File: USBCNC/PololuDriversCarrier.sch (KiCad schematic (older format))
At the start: 10 parts, among them M1 Pololu_A4988, M2 Pololu_A4988, M3 Pololu_A4988, M4 Pololu_A4988, M5 Pololu_A4988

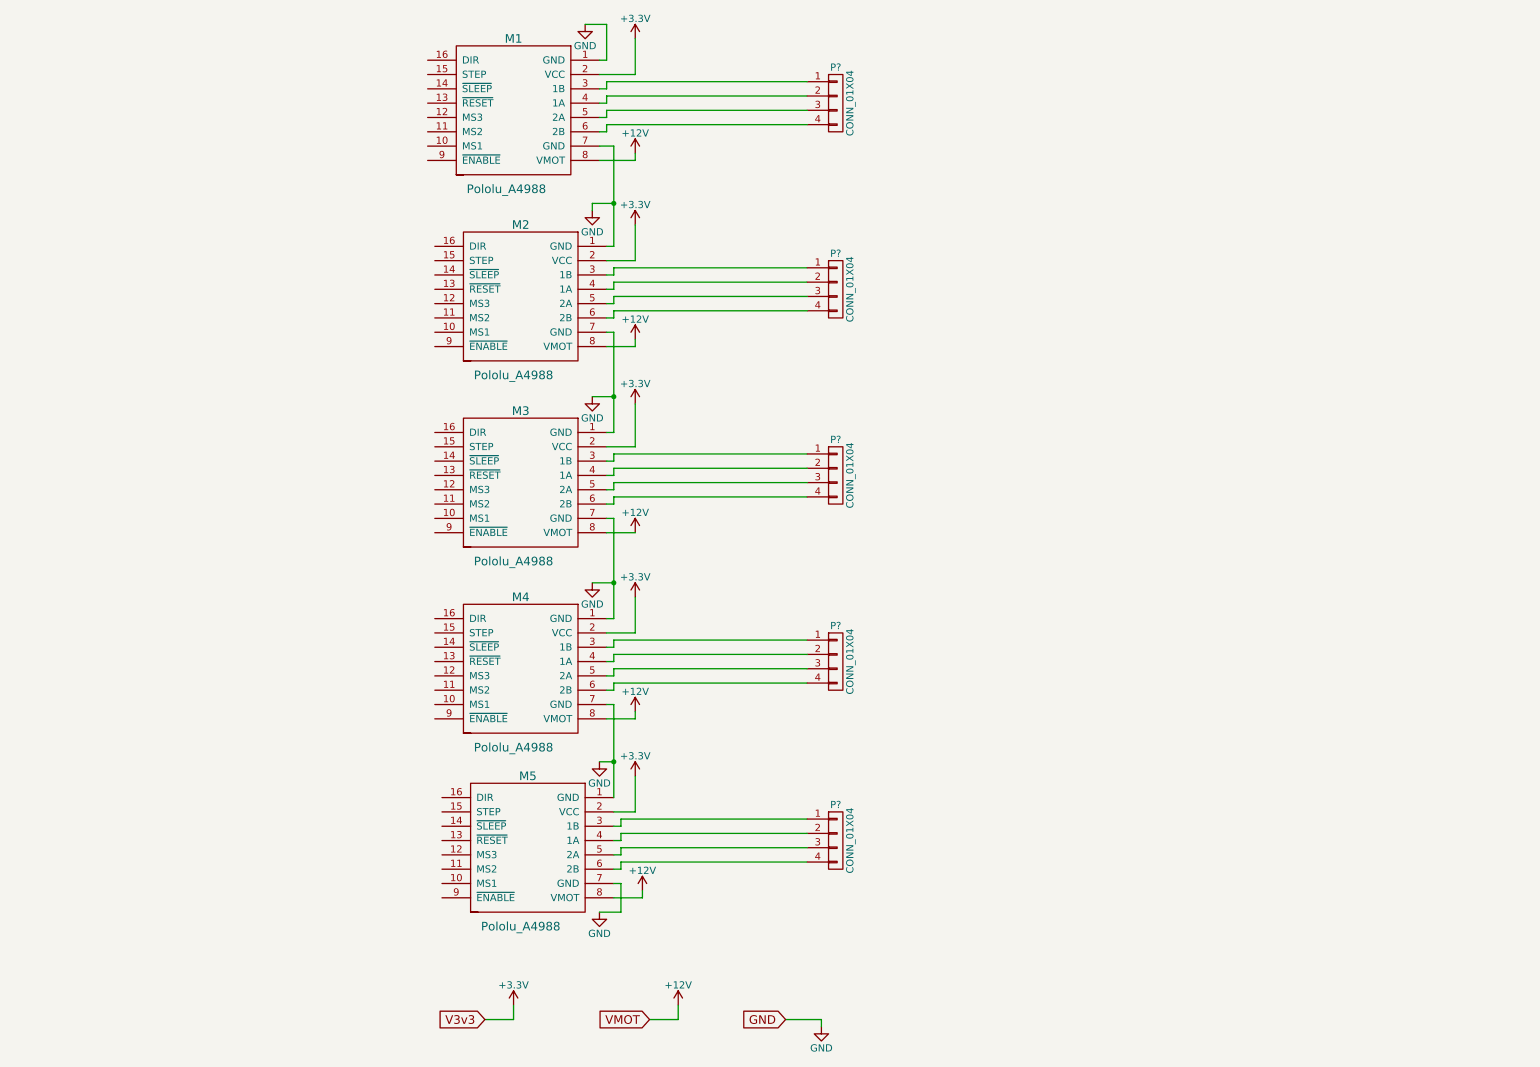
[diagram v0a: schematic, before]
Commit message: Added Pololu module interface
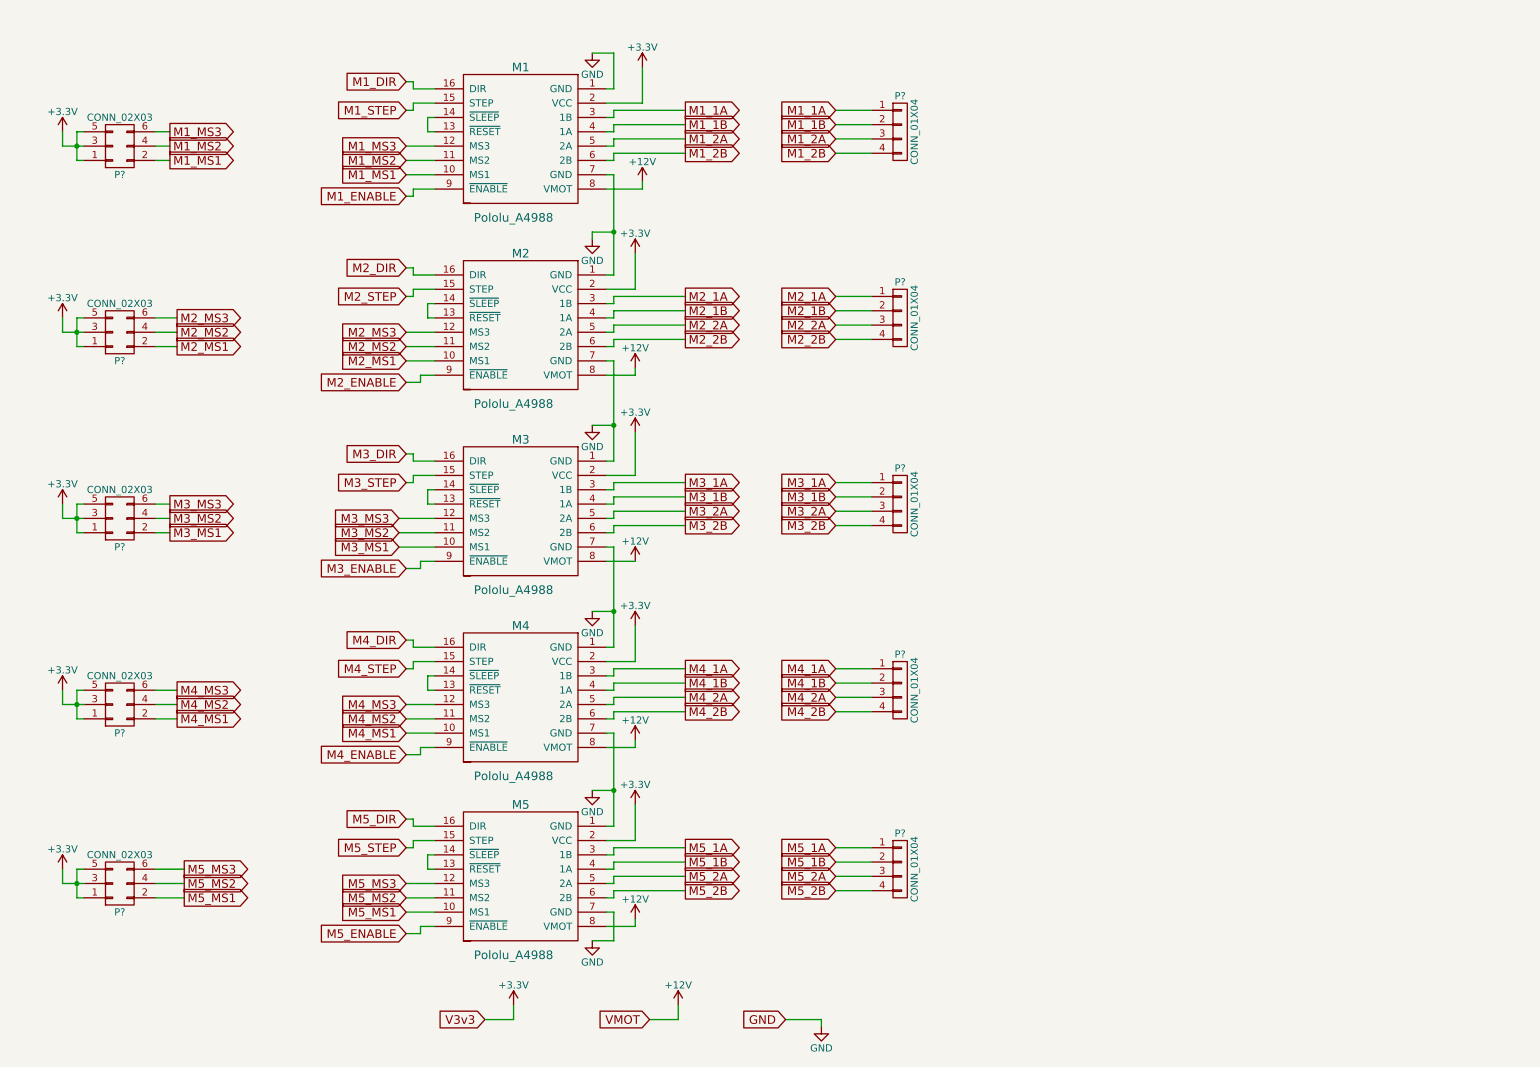
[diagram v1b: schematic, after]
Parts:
- removed P? (x4): CONN_01X04, symbol CONN_01X04
- added P? (x4): CONN_01X04, symbol CONN_01X04
- added P? (x5): CONN_02X03, symbol CONN_02X03
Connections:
- net +3V3: now also P?.1 (P1), P?.1 (P1), P?.1 (P1), P?.1 (P1), P?.1 (P1), P?.3 (P3), P?.3 (P3), P?.3 (P3), P?.3 (P3), P?.3 (P3), P?.5 (P5), P?.5 (P5), P?.5 (P5), P?.5 (P5), P?.5 (P5)
- net M3_MS1: now reaches M3.10 (MS1)
- net M3_MS1: now also P?.2 (P2)
- net M3_MS2: now reaches M3.11 (MS2)
- net M3_MS2: now also P?.4 (P4)
- net M3_MS3: now reaches M3.12 (MS3)
- net M3_MS3: now also P?.6 (P6)
- net at M3.13 (~RESET): now also M3.14 (~SLEEP)
- net M3_STEP: now reaches M3.15 (STEP)
- net M3_DIR: now reaches M3.16 (DIR)
- net M3_1A: now reaches M3.3 (1B)
- net M3_1A: now also P?.1 (P1)
- net M3_1B: now reaches M3.4 (1A)
- net M3_1B: now also P?.2 (P2)
- net M3_2A: now reaches M3.5 (2A)
- net M3_2A: now also P?.3 (P3)
- net M3_2B: now reaches M3.6 (2B)
- net M3_2B: now also P?.4 (P4)
- net M3_ENABLE: now reaches M3.9 (~ENABLE)
- net M5_MS1: now reaches M5.10 (MS1)
- net M5_MS1: now also P?.2 (P2)
- net M5_MS2: now reaches M5.11 (MS2)
- net M5_MS2: now also P?.4 (P4)
- net M5_MS3: now reaches M5.12 (MS3)
- net M5_MS3: now also P?.6 (P6)
- net at M5.13 (~RESET): now also M5.14 (~SLEEP)
- net M5_STEP: now reaches M5.15 (STEP)
- net M5_DIR: now reaches M5.16 (DIR)
- net M5_1A: now reaches M5.3 (1B), P?.1 (P1)
- net M5_1B: now reaches M5.4 (1A), P?.2 (P2)
- net M5_2A: now reaches M5.5 (2A), P?.3 (P3)
- net M5_2B: now reaches M5.6 (2B), P?.4 (P4)
- net M5_ENABLE: now reaches M5.9 (~ENABLE)
- net M4_MS1: now reaches M4.10 (MS1)
- net M4_MS1: now also P?.2 (P2)
- net M4_MS2: now reaches M4.11 (MS2)
- net M4_MS2: now also P?.4 (P4)
- net M4_MS3: now reaches M4.12 (MS3)
- net M4_MS3: now also P?.6 (P6)
- net at M4.13 (~RESET): now also M4.14 (~SLEEP)
- net M4_STEP: now reaches M4.15 (STEP)
- net M4_DIR: now reaches M4.16 (DIR)
- net M4_1A: now reaches M4.3 (1B)
- net M4_1A: now also P?.1 (P1)
- net M4_1B: now reaches M4.4 (1A)
- net M4_1B: now also P?.2 (P2)
- net M4_2A: now reaches M4.5 (2A)
- net M4_2A: now also P?.3 (P3)
- net M4_2B: now reaches M4.6 (2B)
- net M4_2B: now also P?.4 (P4)
- net M4_ENABLE: now reaches M4.9 (~ENABLE)
- net M2_MS1: now reaches M2.10 (MS1)
- net M2_MS1: now also P?.2 (P2)
- net M2_MS2: now reaches M2.11 (MS2)
- net M2_MS2: now also P?.4 (P4)
- net M2_MS3: now reaches M2.12 (MS3)
- net M2_MS3: now also P?.6 (P6)
- net at M2.13 (~RESET): now also M2.14 (~SLEEP)
- net M2_STEP: now reaches M2.15 (STEP)
- net M2_DIR: now reaches M2.16 (DIR)
- net M2_1A: now reaches M2.3 (1B)
- net M2_1A: now also P?.1 (P1)
- net M2_1B: now reaches M2.4 (1A)
- net M2_1B: now also P?.2 (P2)
- net M2_2A: now reaches M2.5 (2A)
- net M2_2A: now also P?.3 (P3)
- net M2_2B: now reaches M2.6 (2B)
- net M2_2B: now also P?.4 (P4)
- net M2_ENABLE: now reaches M2.9 (~ENABLE)
- net M1_MS1: now reaches M1.10 (MS1)
- net M1_MS1: now also P?.2 (P2)
- net M1_MS2: now reaches M1.11 (MS2)
- net M1_MS2: now also P?.4 (P4)
- net M1_MS3: now reaches M1.12 (MS3)
- net M1_MS3: now also P?.6 (P6)
- net at M1.13 (~RESET): now also M1.14 (~SLEEP)
- net M1_STEP: now reaches M1.15 (STEP)
- net M1_DIR: now reaches M1.16 (DIR)
- net M1_1A: now reaches M1.3 (1B)
- net M1_1A: now also P?.1 (P1)
- net M1_1B: now reaches M1.4 (1A)
- net M1_1B: now also P?.2 (P2)
- net M1_2A: now reaches M1.5 (2A)
- net M1_2A: now also P?.3 (P3)
- net M1_2B: now reaches M1.6 (2B)
- net M1_2B: now also P?.4 (P4)
- net M1_ENABLE: now reaches M1.9 (~ENABLE)
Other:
- moved on the sheet: M1, M2, M3, M4, M5, P?

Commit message: Completed the DRV8825 Block(s), and reorganized the pololu blocks
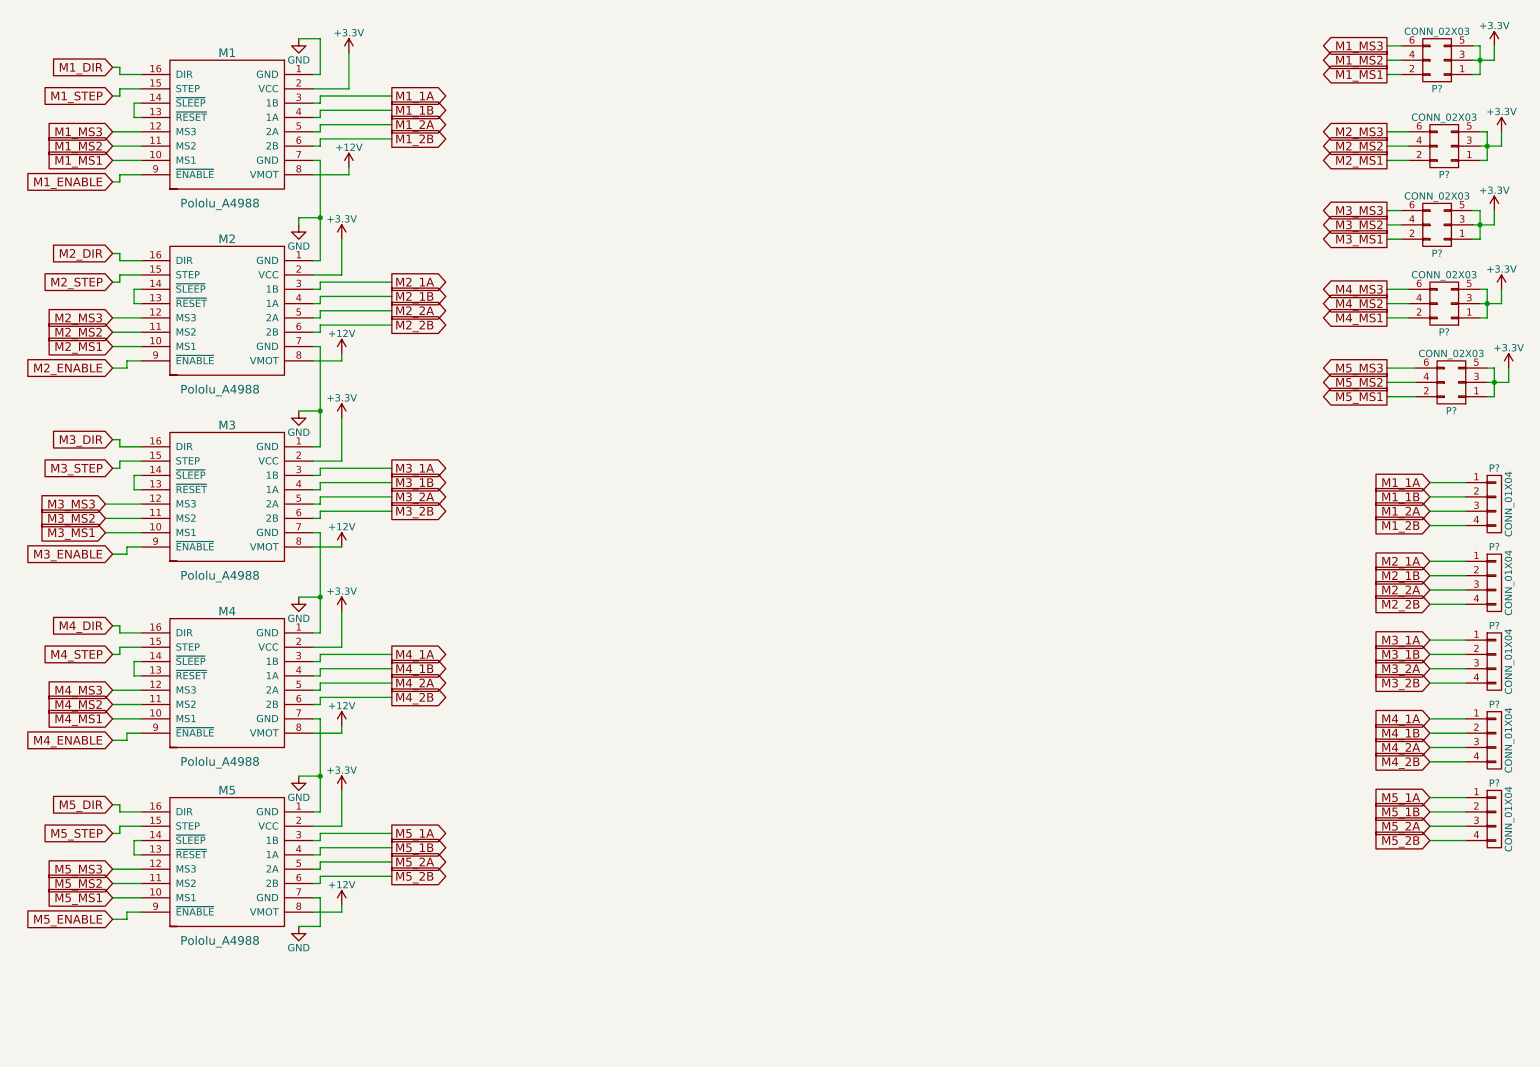
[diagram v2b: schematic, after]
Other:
- moved on the sheet: M1, M2, M3, M4, M5, P?

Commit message: Fixing ERC
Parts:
- added P12, P13, P14, P15, P16, P17, P18, P19: CONN_01X03, symbol CONN_01X03
- added P21: CONN_02X04, symbol CONN_02X04
- gave numbers to parts that had none: 10
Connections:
- net +3V3: now also P12.1 (P1), P13.1 (P1), P14.1 (P1), P15.1 (P1), P16.1 (P1), P17.1 (P1), P18.1 (P1), P19.1 (P1)
- net GND: now also P12.3 (P3), P13.3 (P3), P14.3 (P3), P15.3 (P3), P16.3 (P3), P17.3 (P3), P18.3 (P3), P19.3 (P3)
- new net M1-MAX: P13.2 (P2), P21.6 (P6)
- new net M1-MIN: P15.2 (P2), P21.2 (P2)
- new net M2-MAX: P12.2 (P2), P21.8 (P8)
- new net M2-MIN: P14.2 (P2), P21.4 (P4)
- new net M3-MAX: P18.2 (P2)
- new net M3-MIN: P19.2 (P2)
- new net M4-MAX: P16.2 (P2), P21.5 (P5), P21.7 (P7)
- new net M4-MIN: P17.2 (P2), P21.1 (P1), P21.3 (P3)
